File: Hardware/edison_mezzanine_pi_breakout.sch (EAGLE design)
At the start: 42 parts, among them U1 PCA9306, U2 EDISON_CONNECTOR_FULLMOUNTING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, U3 EDISON_CONNECTOR_FULLHEADER, U4 TPS62065, U5 MIC5219 3.3V

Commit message: Initial component placement.
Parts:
- added R10: 22, SparkFun-Resistors:22OHM1/10W1%(0603)
- added R9: 10K, SparkFun-Resistors:10KOHM1/10W1%(0603)0603
- added S1: POWER, SparkFun-Electromechanical:SWITCH-MOMENTARY-2-SMD-1101NE
- renumbered R13 to R7, R14 to R8
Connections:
- new net N$15: R10.2, R9.2, S1.1
- net GND: now also S1.2
- net PWRBTN#: now also R10.1
- net VSYS: now also R9.1
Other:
- note added: "Power Button"
- moved on the sheet: F1, JP3
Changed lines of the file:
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@@
 <part name="GND22" library="SparkFun-Aesthetics" deviceset="GND" device=""/>
 <part name="SUPPLY11" library="SparkFun-Aesthetics" deviceset="5V" device=""/>
-<part name="R13" library="SparkFun-Resistors" deviceset="RESISTOR" device="0603" value="680k"/>
-<part name="R14" library="SparkFun-Resistors" deviceset="RESISTOR" device="0603" value="120k"/>
+<part name="R7" library="SparkFun-Resistors" deviceset="RESISTOR" device="0603" value="680k"/>
+<part name="R8" library="SparkFun-Resistors" deviceset="RESISTOR" device="0603" value="120k"/>
 <part name="C9" library="SparkFun-Capacitors" deviceset="9.0PF-50V-10%(0603)" device="" value="9.0pF"/>
 <part name="C10" library="SparkFun-Capacitors" deviceset="4.7UF-6.3V-10%(0603)" device="0603" value="4.7uF"/>
@@
 <part name="GND24" library="SparkFun-Aesthetics" deviceset="GND" device=""/>
 <part name="GND25" library="SparkFun-Aesthetics" deviceset="GND" device=""/>
+<part name="S1" library="SparkFun-Electromechanical" deviceset="SWITCH-MOMENTARY-2" device="-SMD-1101NE" value="POWER"/>
+<part name="R9" library="SparkFun-Resistors" deviceset="10KOHM1/10W1%(0603)" device="0603" value="10K"/>
+<part name="R10" library="SparkFun-Resistors" deviceset="22OHM1/10W1%(0603)" device="" value="22"/>
+<part name="GND26" library="SparkFun-Aesthetics" deviceset="GND" device=""/>
 </parts>
 <sheets>
@@
 <wire x1="114.3" y1="144.78" x2="114.3" y2="154.94" width="0.1524" layer="97" style="longdash"/>
 <wire x1="114.3" y1="154.94" x2="114.3" y2="185.42" width="0.1524" layer="97" style="longdash"/>
-<wire x1="114.3" y1="154.94" x2="0" y2="154.94" width="0.1524" layer="97" style="longdash"/>
+<wire x1="114.3" y1="154.94" x2="50.8" y2="154.94" width="0.1524" layer="97" style="longdash"/>
+<wire x1="50.8" y1="154.94" x2="0" y2="154.94" width="0.1524" layer="97" style="longdash"/>
 <wire x1="114.3" y1="71.12" x2="0" y2="71.12" width="0.1524" layer="97" style="longdash"/>
 <wire x1="246.38" y1="99.06" x2="0" y2="99.06" width="0.1524" layer="97" style="longdash"/>
@@
 <wire x1="114.3" y1="35.56" x2="60.96" y2="35.56" width="0.1524" layer="97" style="longdash"/>
 <wire x1="60.96" y1="0" x2="60.96" y2="35.56" width="0.1524" layer="97" style="longdash"/>
+<wire x1="50.8" y1="154.94" x2="50.8" y2="185.42" width="0.1524" layer="97" style="longdash"/>
+<text x="51.816" y="155.956" size="2.032" layer="97">Power Button</text>
 </plain>
 <instances>
@@
 <instance part="GND6" gate="1" x="223.52" y="63.5"/>
 <instance part="SUPPLY1" gate="G$1" x="223.52" y="81.28"/>
-<instance part="F1" gate="G$1" x="71.12" y="175.26"/>
-<instance part="JP3" gate="G$1" x="53.34" y="170.18" rot="MR0"/>
-<instance part="GND7" gate="1" x="63.5" y="160.02" rot="MR0"/>
-<instance part="GND8" gate="1" x="43.18" y="170.18" rot="MR90"/>
-<instance part="SUPPLY3" gate="G$1" x="81.28" y="177.8"/>
+<instance part="F1" gate="G$1" x="35.56" y="175.26"/>
+<instance part="JP3" gate="G$1" x="17.78" y="170.18" rot="MR0"/>
+<instance part="GND7" gate="1" x="27.94" y="160.02" rot="MR0"/>
+<instance part="GND8" gate="1" x="5.08" y="165.1" rot="MR0"/>
+<instance part="SUPPLY3" gate="G$1" x="45.72" y="177.8"/>
 <instance part="R6" gate="G$1" x="96.52" y="127" rot="R90"/>
 <instance part="D3" gate="G$1" x="96.52" y="139.7"/>
@@
 <instance part="GND22" gate="1" x="48.26" y="124.46"/>
 <instance part="SUPPLY11" gate="G$1" x="7.62" y="147.32"/>
-<instance part="R13" gate="G$1" x="66.04" y="137.16" rot="R90"/>
-<instance part="R14" gate="G$1" x="66.04" y="119.38" rot="R90"/>
+<instance part="R7" gate="G$1" x="66.04" y="137.16" rot="R90"/>
+<instance part="R8" gate="G$1" x="66.04" y="119.38" rot="R90"/>
 <instance part="C9" gate="G$1" x="73.66" y="134.62"/>
 <instance part="C10" gate="G$1" x="7.62" y="134.62"/>
@@
 <instance part="GND24" gate="1" x="83.82" y="48.26"/>
 <instance part="GND25" gate="1" x="96.52" y="48.26"/>
+<instance part="S1" gate="G$1" x="93.98" y="167.64"/>
+<instance part="R9" gate="G$1" x="91.44" y="177.8" smashed="yes" rot="R180">
+<attribute name="NAME" x="95.25" y="181.3814" size="1.778" layer="95" rot="R180"/>
+<attribute name="VALUE" x="95.25" y="176.022" size="1.778" layer="96" rot="R180"/>
+</instance>
+<instance part="R10" gate="G$1" x="78.74" y="167.64"/>
+<instance part="GND26" gate="1" x="101.6" y="162.56"/>
 </instances>
 <busses>
@@
 <pinref part="JP3" gate="G$1" pin="GND"/>
 <pinref part="GND7" gate="1" pin="GND"/>
-<wire x1="60.96" y1="165.1" x2="63.5" y2="165.1" width="0.1524" layer="91"/>
-<wire x1="63.5" y1="165.1" x2="63.5" y2="162.56" width="0.1524" layer="91"/>
-</segment>
-<segment>
-<pinref part="JP3" gate="G$1" pin="SHIELD"/>
-<pinref part="GND8" gate="1" pin="GND"/>
+<wire x1="25.4" y1="165.1" x2="27.94" y2="165.1" width="0.1524" layer="91"/>
+<wire x1="27.94" y1="165.1" x2="27.94" y2="162.56" width="0.1524" layer="91"/>
 </segment>
 <segment>
@@
 </segment>
 <segment>
-<pinref part="R14" gate="G$1" pin="1"/>
+<pinref part="R8" gate="G$1" pin="1"/>
 <pinref part="GND19" gate="1" pin="GND"/>
 <wire x1="66.04" y1="111.76" x2="66.04" y2="114.3" width="0.1524" layer="91"/>
@@
 <pinref part="GND25" gate="1" pin="GND"/>
 </segment>
+<segment>
+<pinref part="S1" gate="G$1" pin="2"/>
+<wire x1="99.06" y1="167.64" x2="101.6" y2="167.64" width="0.1524" layer="91"/>
+<wire x1="101.6" y1="167.64" x2="101.6" y2="165.1" width="0.1524" layer="91"/>
+<pinref part="GND26" gate="1" pin="GND"/>
+</segment>
+<segment>
+<pinref part="GND8" gate="1" pin="GND"/>
+<wire x1="5.08" y1="167.64" x2="5.08" y2="170.18" width="0.1524" layer="91"/>
+<pinref part="JP3" gate="G$1" pin="SHIELD"/>
+<wire x1="5.08" y1="170.18" x2="10.16" y2="170.18" width="0.1524" layer="91"/>
+</segment>
 </net>
 <net name="1.8V" class="0">
@@
 <pinref part="C9" gate="G$1" pin="1"/>
 <wire x1="73.66" y1="144.78" x2="73.66" y2="139.7" width="0.1524" layer="91"/>
-<pinref part="R13" gate="G$1" pin="2"/>
+<pinref part="R7" gate="G$1" pin="2"/>
 <wire x1="73.66" y1="144.78" x2="66.04" y2="144.78" width="0.1524" layer="91"/>
 <wire x1="66.04" y1="144.78" x2="63.5" y2="144.78" width="0.1524" layer="91"/>
@@
 <label x="35.56" y="91.44" size="1.27" layer="95" rot="R180" xref="yes"/>
 </segment>
+<segment>
+<wire x1="96.52" y1="177.8" x2="99.06" y2="177.8" width="0.1524" layer="91"/>
+<pinref part="R9" gate="G$1" pin="1"/>
+<label x="99.06" y="177.8" size="1.778" layer="95" xref="yes"/>
+</segment>
 </net>
 <net name="N$2" class="0">
 <segment>
 <pinref part="JP3" gate="G$1" pin="VCC"/>
-<wire x1="60.96" y1="175.26" x2="66.04" y2="175.26" width="0.1524" layer="91"/>
+<wire x1="25.4" y1="175.26" x2="30.48" y2="175.26" width="0.1524" layer="91"/>
 <pinref part="F1" gate="G$1" pin="1"/>
 </segment>
@@
 <pinref part="F1" gate="G$1" pin="2"/>
 <pinref part="SUPPLY3" gate="G$1" pin="5V"/>
-<wire x1="78.74" y1="175.26" x2="81.28" y2="175.26" width="0.1524" layer="91"/>
-<wire x1="81.28" y1="175.26" x2="81.28" y2="177.8" width="0.1524" layer="91"/>
+<wire x1="43.18" y1="175.26" x2="45.72" y2="175.26" width="0.1524" layer="91"/>
+<wire x1="45.72" y1="175.26" x2="45.72" y2="177.8" width="0.1524" layer="91"/>
 </segment>
 <segment>
@@
 <net name="N$18" class="0">
 <segment>
-<pinref part="R13" gate="G$1" pin="1"/>
-<pinref part="R14" gate="G$1" pin="2"/>
+<pinref part="R7" gate="G$1" pin="1"/>
+<pinref part="R8" gate="G$1" pin="2"/>
 <wire x1="66.04" y1="124.46" x2="66.04" y2="127" width="0.1524" layer="91"/>
 <pinref part="C9" gate="G$1" pin="2"/>
@@
 </segment>
 </net>
+<net name="N$15" class="0">
+<segment>
+<pinref part="R10" gate="G$1" pin="2"/>
+<pinref part="R9" gate="G$1" pin="2"/>
+<wire x1="83.82" y1="167.64" x2="86.36" y2="167.64" width="0.1524" layer="91"/>
+<wire x1="86.36" y1="167.64" x2="86.36" y2="177.8" width="0.1524" layer="91"/>
+<pinref part="S1" gate="G$1" pin="1"/>
+<wire x1="86.36" y1="167.64" x2="88.9" y2="167.64" width="0.1524" layer="91"/>
+<junction x="86.36" y="167.64"/>
+</segment>
+</net>
+<net name="PWRBTN#" class="0">
+<segment>
+<pinref part="R10" gate="G$1" pin="1"/>
+<wire x1="73.66" y1="167.64" x2="71.12" y2="167.64" width="0.1524" layer="91"/>
+<label x="71.12" y="167.64" size="1.778" layer="95" rot="R180" xref="yes"/>
+</segment>
+</net>

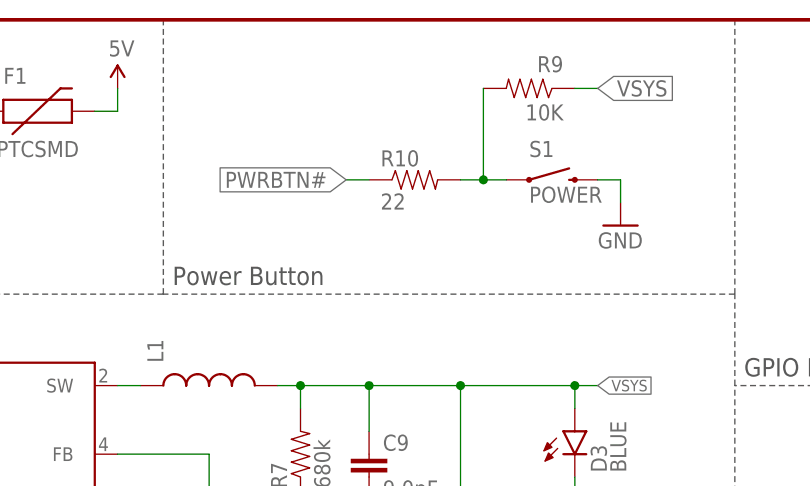
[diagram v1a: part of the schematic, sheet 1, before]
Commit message: More layout. Swapped 22 Ohm with 220 Ohm in schematic for power button.
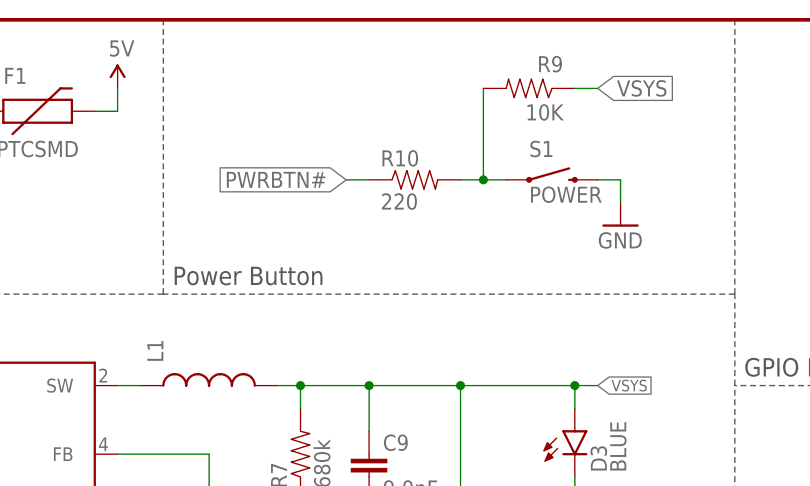
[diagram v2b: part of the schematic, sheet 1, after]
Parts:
- R10: value 22 -> 220; device SparkFun-Resistors:22OHM1/10W1%(0603) -> SparkFun-Resistors:RESISTOR0603; PROD_ID (none) -> RES-07861
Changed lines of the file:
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@@
 <setting verticaltext="up"/>
 </settings>
-<grid distance="0.1" unitdist="inch" unit="inch" style="lines" multiple="1" display="yes" altdistance="0.01" altunitdist="inch" altunit="inch"/>
+<grid distance="0.1" unitdist="inch" unit="inch" style="lines" multiple="1" display="no" altdistance="0.01" altunitdist="inch" altunit="inch"/>
 <layers>
 <layer number="1" name="Top" color="4" fill="1" visible="no" active="no"/>
@@
 <part name="S1" library="SparkFun-Electromechanical" deviceset="SWITCH-MOMENTARY-2" device="-SMD-1101NE" value="POWER"/>
 <part name="R9" library="SparkFun-Resistors" deviceset="10KOHM1/10W1%(0603)" device="0603" value="10K"/>
-<part name="R10" library="SparkFun-Resistors" deviceset="22OHM1/10W1%(0603)" device="" value="22"/>
+<part name="R10" library="SparkFun-Resistors" deviceset="RESISTOR" device="0603" value="220">
+<attribute name="PROD_ID" value="RES-07861"/>
+</part>
 <part name="GND26" library="SparkFun-Aesthetics" deviceset="GND" device=""/>
 </parts>
@@
 <attribute name="VALUE" x="95.25" y="176.022" size="1.778" layer="96" rot="R180"/>
 </instance>
-<instance part="R10" gate="G$1" x="78.74" y="167.64"/>
+<instance part="R10" gate="G$1" x="78.74" y="167.64">
+<attribute name="PROD_ID" x="78.74" y="167.64" size="1.778" layer="96" display="off"/>
+</instance>
 <instance part="GND26" gate="1" x="101.6" y="162.56"/>
 </instances>

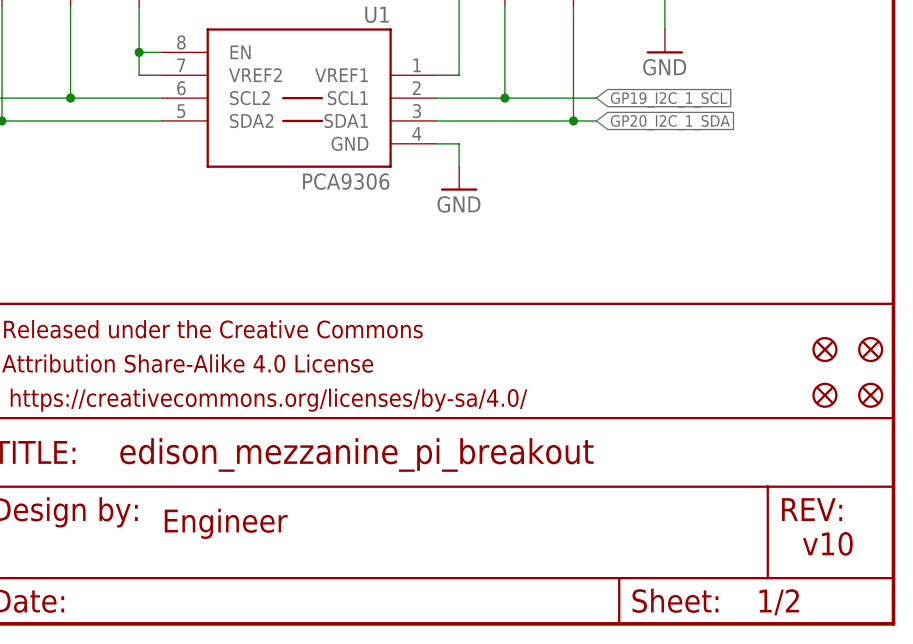
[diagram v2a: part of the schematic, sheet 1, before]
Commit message: Finished layout for prototype.
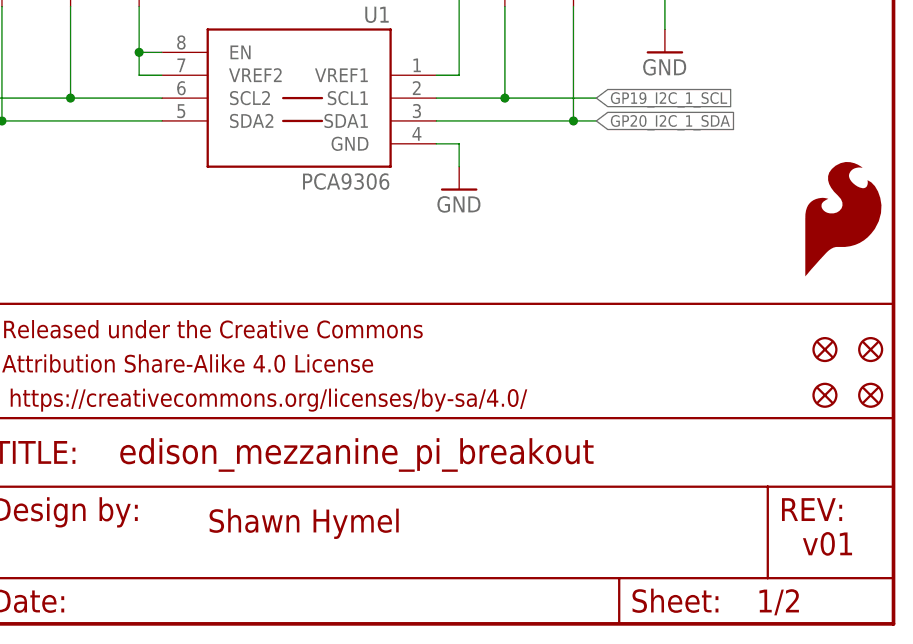
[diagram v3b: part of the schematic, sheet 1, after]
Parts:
- added LOGO3: SFE_LOGO_FLAME.1_INCH, SparkFun-Aesthetics:SFE_LOGO_FLAME.1_INCH
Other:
- note added: "Shawn Hymel"
- note added: "v01"
- note removed: "Engineer"
- note removed: "v10"
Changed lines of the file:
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@@
 </part>
 <part name="GND26" library="SparkFun-Aesthetics" deviceset="GND" device=""/>
+<part name="LOGO3" library="SparkFun-Aesthetics" deviceset="SFE_LOGO_FLAME" device=".1_INCH"/>
 </parts>
 <sheets>
 <sheet>
 <plain>
-<text x="238.76" y="7.62" size="2.54" layer="94">v10</text>
-<text x="167.64" y="10.16" size="2.54" layer="94">Engineer</text>
+<text x="238.76" y="7.62" size="2.54" layer="94">v01</text>
+<text x="172.72" y="10.16" size="2.54" layer="94">Shawn Hymel</text>
 <wire x1="114.3" y1="35.56" x2="114.3" y2="71.12" width="0.1524" layer="97" style="longdash"/>
 <wire x1="114.3" y1="71.12" x2="114.3" y2="144.78" width="0.1524" layer="97" style="longdash"/>
@@
 </instance>
 <instance part="GND26" gate="1" x="101.6" y="162.56"/>
+<instance part="LOGO3" gate="G$1" x="238.76" y="38.1"/>
 </instances>
 <busses>
